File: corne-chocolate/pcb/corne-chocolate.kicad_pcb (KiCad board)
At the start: 2 copper layers, 133.8 x 91.4 mm, 98 parts, among them J1 MJ-4PP-9, J2 Conn_01x04, J3 LED, P1 i2c-pin, P2 i2c-pin, SW1 SW_PUSH, SW10 SW_PUSH, SW11 SW_PUSH, SW12 SW_PUSH, SW13 SW_PUSH, SW14 SW_PUSH, SW15 SW_PUSH, SW16 SW_PUSH, SW17 SW_PUSH, SW18 SW_PUSH, SW19 SW_PUSH, SW2 SW_PUSH, SW20 SW_PUSH, SW21 SW_PUSH, SW3 SW_PUSH, SW4 SW_PUSH, SW5 SW_PUSH, SW6 SW_PUSH, SW7 SW_PUSH, SW8 SW_PUSH, SW9 SW_PUSH, U1 ProMicro

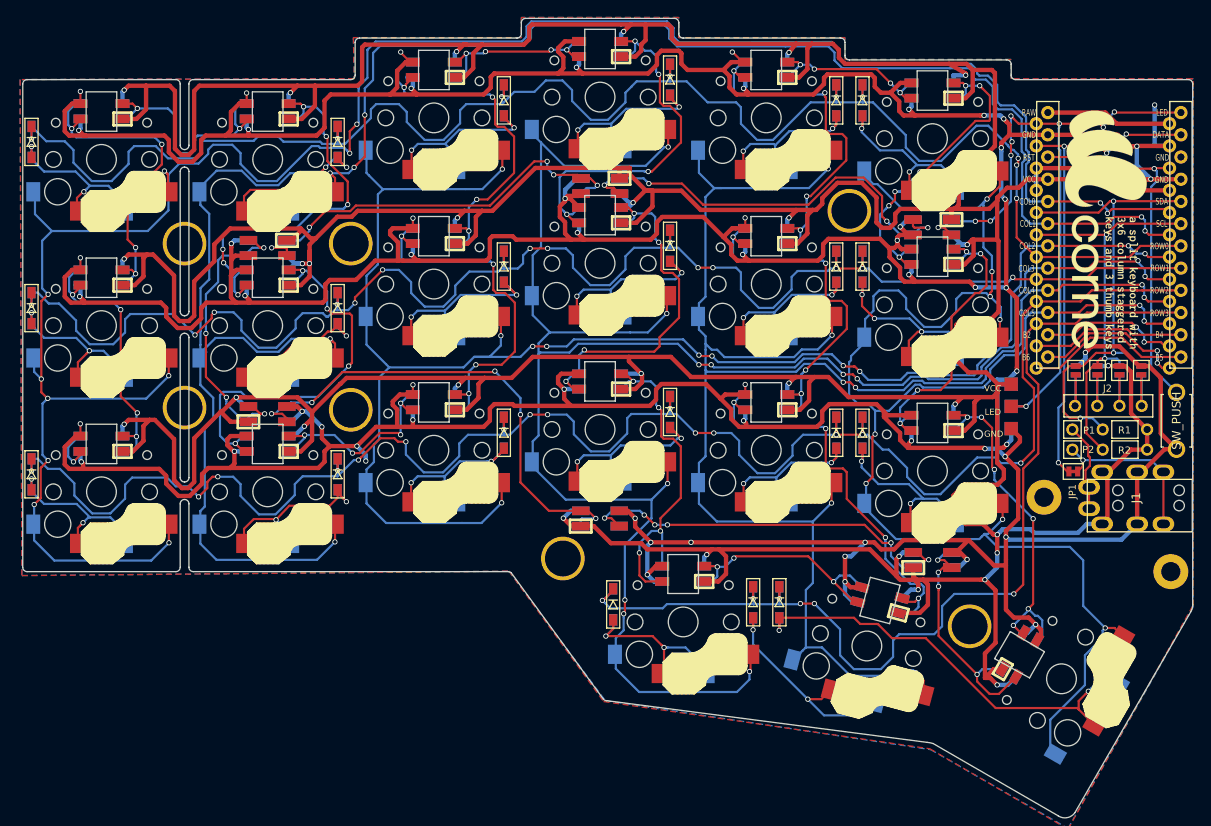
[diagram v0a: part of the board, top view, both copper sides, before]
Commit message: starts non-reversable pcbs routing
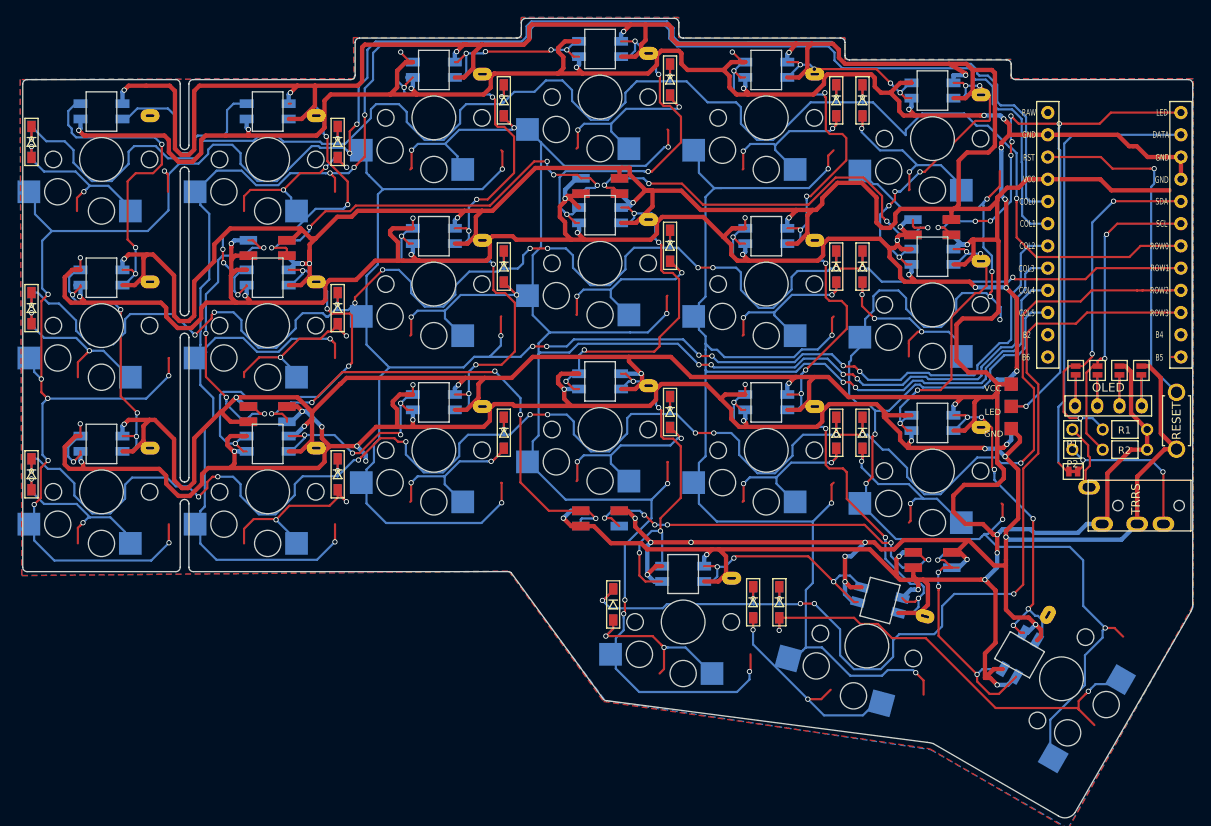
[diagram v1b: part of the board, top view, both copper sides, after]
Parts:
- removed ? (x9): , kbd:LEGO_HOLE
- removed G*** (x2): LOGO, kbd:corne
- removed JP6, JP7, JP8, JP9: , kbd:Jumper
- J1: footprint kbd:MJ-4PP-9 -> kbd:MJ-4PP-9_1side
- J2: footprint kbd:OLED -> kbd:OLED_1side
- J3: value LED -> Conn_01x03
- JP1: value (none) -> Device:Jumper
- JP2, JP3, JP4, JP5: value (none) -> Device:Jumper_NO_Small
- P1, P2: value i2c-pin -> Conn_01x01
- RSW1: footprint kbd:ResetSW -> kbd:ResetSW_1side
- SW1, SW10, SW11, SW12, SW13, SW14, SW15, SW16, SW17, SW18, SW19, SW2, SW20, SW3, SW4, SW5, SW6, SW7, SW8, SW9: footprint kbd:Choc_Hotswap -> kbd:ChocV1_V2_Hotswap
- SW21: footprint kbd:Choc_Hotswap_1.5u -> kbd:ChocV1_V2_Hotswap_1.5u
- U1: footprint kbd:ProMicro_v2 -> kbd:ProMicro_v2_1side
- turned SW1 to 0 degrees
- turned SW10 to 0 degrees
- turned SW11 to 0 degrees
- turned SW12 to 0 degrees
- turned SW13 to 0 degrees
- turned SW14 to 0 degrees
- turned SW15 to 0 degrees
- turned SW16 to 0 degrees
- turned SW17 to 0 degrees
- turned SW18 to 0 degrees
- turned SW19 to 0 degrees
- turned SW2 to 0 degrees
- turned SW20 to -15 degrees
- turned SW21 to 60 degrees
- turned SW3 to 0 degrees
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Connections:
- L13 pad 1: Net-(L13-Pad1) -> unconnected-(L13-DOUT-Pad1)
- U1 pad 11: Net-(U1-Pad11) -> unconnected-(U1-8/B4-Pad11)
- U1 pad 12: Net-(U1-Pad12) -> unconnected-(U1-9/B5-Pad12)
- U1 pad 13: Net-(U1-Pad13) -> unconnected-(U1-B6/10-Pad13)
- U1 pad 14: Net-(U1-Pad14) -> unconnected-(U1-B2/16-Pad14)
- U1 pad 24: Net-(U1-Pad24) -> unconnected-(U1-RAW-Pad24)
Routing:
- net (no net): track 0.00 -> 298.9 mm, vias 0 -> 35
- net GND: track 816.7 -> 759.8 mm, vias 59 -> 53
- net Net-(L14-DOUT): track 45.6 -> 0.00 mm, vias 4 -> 0
- net Net-(L2-DIN): track 46.2 -> 1.10 mm, vias 6 -> 0
- net Net-(L10-DOUT): track 42.9 -> 0.00 mm, vias 4 -> 0
- net Net-(L10-DIN): track 39.7 -> 0.00 mm, vias 4 -> 0
- net Net-(L16-DIN): track 39.3 -> 0.00 mm, vias 4 -> 0
- net Net-(L12-DOUT): track 37.0 -> 0.00 mm, vias 6 -> 0
- net Net-(L12-DIN): track 34.5 -> 0.00 mm, vias 4 -> 0
- net Net-(L5-DIN): track 19.8 -> 0.00 mm, vias 4 -> 0
- net Net-(U1-Pad12): track 18.9 -> 0.00 mm
- net col5: track 188.2 -> 170.3 mm, vias 10 -> 8
- net Net-(U1-Pad11): track 17.6 -> 0.00 mm
- net Net-(U1-Pad13): track 17.5 -> 0.00 mm, vias 2 -> 0
- net Net-(U1-Pad14): track 16.0 -> 0.00 mm, vias 2 -> 0
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
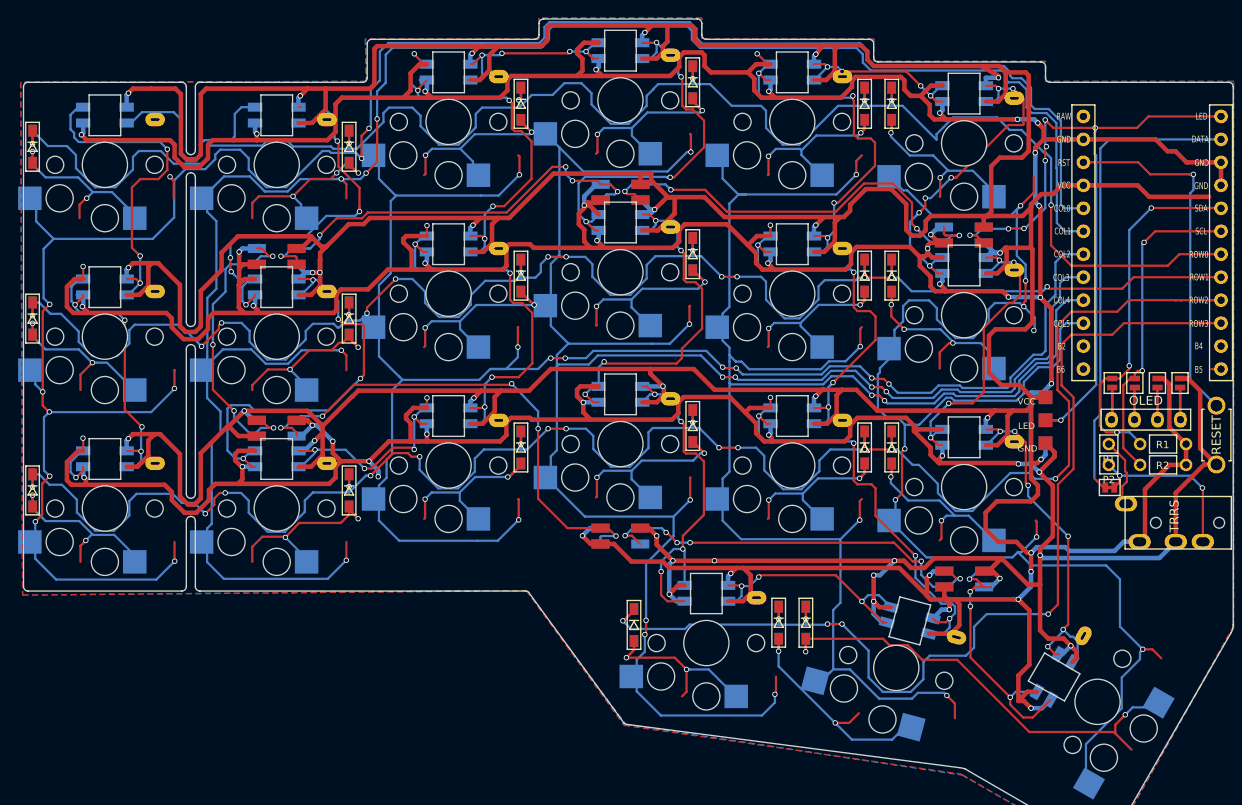
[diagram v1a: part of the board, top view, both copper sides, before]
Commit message: removes all reversible routing
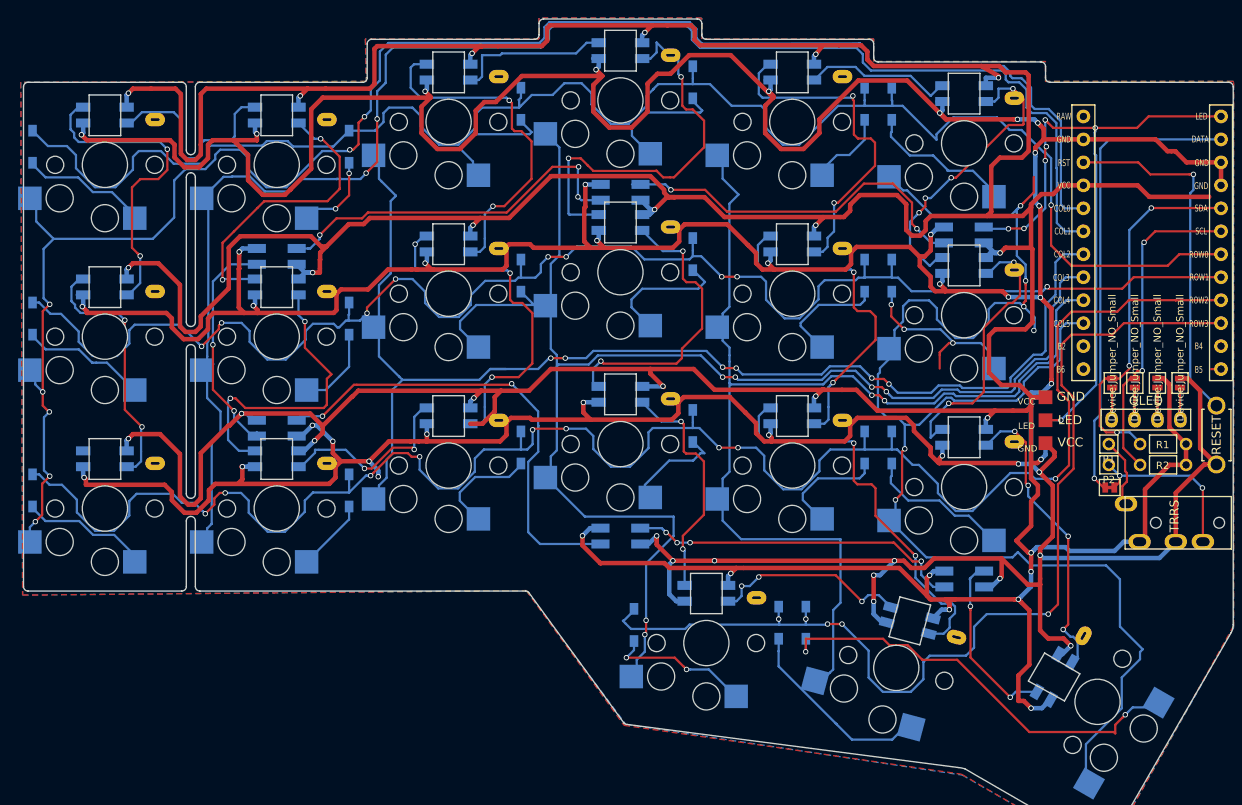
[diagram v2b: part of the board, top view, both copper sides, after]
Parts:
- J3: footprint kbd:StripLED_rev -> kbd:StripLED_1side
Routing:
- net (no net): track 298.9 -> 0.00 mm, vias 35 -> 0
- net VCC: track 777.0 -> 655.3 mm, vias 29 -> 28
- net GND: track 759.8 -> 691.4 mm, vias 53 -> 43
- net col3: track 209.1 -> 146.4 mm, vias 10 -> 6
- net col4: track 180.6 -> 122.5 mm, vias 6 -> 2
- net Net-(L10-DOUT): track 0.00 -> 44.4 mm, vias 0 -> 2
- net col2: track 178.9 -> 134.9 mm, vias 9 -> 6
- net col1: track 216.6 -> 172.8 mm, vias 5 -> 2
- net col0: track 239.8 -> 196.9 mm, vias 10 -> 7
- net Net-(L12-DOUT): track 0.00 -> 33.7 mm, vias 0 -> 4
- net Net-(L14-DOUT): track 0.00 -> 33.6 mm, vias 0 -> 2
- net Net-(L10-DIN): track 0.00 -> 32.2 mm, vias 0 -> 2
- net Net-(L2-DIN): track 1.10 -> 32.8 mm, vias 0 -> 2
- net Net-(L12-DIN): track 0.00 -> 30.9 mm, vias 0 -> 2
- net Net-(L16-DIN): track 0.00 -> 26.0 mm, vias 0 -> 2
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
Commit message: starts re-routing. switch to a 3x5 kbd
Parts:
- removed D1, D13, D7: D, kbd:D3_SMD
- removed L1, L13, L7: SK6812MINI, kbd:SK6812MINI_rev
- removed SW1, SW13, SW7: SW_PUSH, kbd:ChocV1_V2_Hotswap
- JP1: footprint kbd:JPC2 -> kbd:Jumper; moved to B.Cu
- moved JP1 1.16 mm to (180.0, 113.0)
- turned JP2 to 90 degrees
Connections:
- J1 pad B: Net-(P2-Pin_1) -> data
- JP1 pad 2: Net-(P2-Pin_1) -> data
- JP2 pad 1: GND -> Net-(J2-Pin_4)
- JP2 pad 2: Net-(J2-Pin_4) -> GND
- L2 pad 1: Net-(L1-DIN) -> unconnected-(L2-DOUT-Pad1)
- P2 pad 1: Net-(P2-Pin_1) -> data
- U1 pad 20: col0 -> unconnected-(U1-F4/A3-Pad20)
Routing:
- net VCC: track 655.3 -> 259.3 mm, vias 28 -> 2
- net GND: track 691.4 -> 340.3 mm, vias 43 -> 12
- net row2: track 199.8 -> 0.00 mm, vias 9 -> 0
- net col0: track 196.9 -> 0.00 mm, vias 7 -> 0
- net row3: track 114.4 -> 0.00 mm, vias 5 -> 0
- net col2: track 134.9 -> 39.0 mm, vias 6 -> 4
- net col5: track 163.2 -> 82.1 mm
- net col3: track 146.4 -> 68.4 mm
- net row1: track 172.3 -> 102.8 mm, vias 9 -> 0
- net row0: track 183.3 -> 115.1 mm, vias 1 -> 2
- net col4: track 122.5 -> 65.5 mm, vias 2 -> 6
- net Net-(L25-DOUT): track 52.9 -> 0.00 mm, vias 2 -> 0
- net Net-(D21-A): track 47.7 -> 0.00 mm, vias 2 -> 0
- net Net-(L10-DOUT): track 44.4 -> 0.00 mm, vias 2 -> 0
- net Net-(L17-DOUT): track 44.2 -> 0.00 mm, vias 2 -> 0
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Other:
- board size 133.8 x 91.4 mm -> 115.3 x 91.4 mm
- rule pad_to_mask_clearance: 0.2 -> 0.0508
- board text removed: "OLED"

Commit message: pcb with ohspark constraints
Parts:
- added G***: LOGO, kbd:corne-logo-horizontal, F.Cu at (106.7, 121.4)
- added H1: MountingHole, MountingHole:MountingHole_2.2mm_M2_ISO14580, F.Cu at (177.8, 115.8)
- added H2: MountingHole, MountingHole:MountingHole_2.2mm_M2_ISO14580, F.Cu at (192.3, 124.2)
- added H3: MountingHole, MountingHole:MountingHole_4.3mm_M4_ISO14580, F.Cu at (98.5, 86.8)
- added H4: MountingHole, MountingHole:MountingHole_4.3mm_M4_ISO14580, F.Cu at (155.5, 83.0)
- added H5: MountingHole, MountingHole:MountingHole_4.3mm_M4_ISO14580, F.Cu at (98.5, 105.8)
- added H6: MountingHole, MountingHole:MountingHole_4.3mm_M4_ISO14580, F.Cu at (122.8, 122.8)
- added H7: MountingHole, MountingHole:MountingHole_4.3mm_M4_ISO14580, F.Cu at (169.3, 130.5)
- L10, L11, L12, L14, L15, L16, L17, L18, L19, L2, L20, L21, L3, L4, L5, L6, L8, L9: footprint kbd:SK6812MINI_rev -> kbd:YS-SK6812MINI-E
- turned P1 to 90 degrees
- turned P2 to 180 degrees
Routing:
- net GND: track 340.3 -> 346.6 mm
- net VCC: track 259.3 -> 264.0 mm
- net col2: track 39.0 -> 40.5 mm
- net row1: track 102.8 -> 101.5 mm
- net col5: track 82.1 -> 83.0 mm
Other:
- board size 115.3 x 91.4 mm -> 116.2 x 91.4 mm
- board text added: "Corne Designed by foostan Remixed by ektocommers"
- board text removed: "Corne Chocolate v2.1 PCB designed by foostan"

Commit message: routing..
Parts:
- removed G***: LOGO, kbd:corne-logo-horizontal
- added kibuzzard-65BBD98A: G***, kibuzzard-65BBD98A, F.Cu at (106.3, 121.8)
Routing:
- net GND: track 346.6 -> 519.5 mm, vias 12 -> 15
- net VCC: track 264.0 -> 406.9 mm, vias 2 -> 7
- net col2: track 40.5 -> 152.6 mm, vias 4 -> 5
- net row2: track 0.00 -> 109.2 mm
- net row3: track 0.00 -> 90.6 mm
- net col3: track 68.2 -> 140.2 mm
- net col4: track 65.5 -> 114.4 mm, vias 6 -> 7
- net Net-(L22-DIN): track 0.50 -> 36.3 mm
- net Net-(L22-DOUT): track 0.00 -> 29.2 mm, vias 0 -> 2
- net Net-(L3-DOUT): track 0.00 -> 28.7 mm, vias 0 -> 2
- net col5: track 83.0 -> 111.2 mm, vias 6 -> 7
- net Net-(L11-DIN): track 0.00 -> 26.7 mm, vias 0 -> 2
- net Net-(L2-DIN): track 0.00 -> 25.8 mm, vias 0 -> 2
- net Net-(L14-DOUT): track 0.30 -> 24.2 mm, vias 0 -> 2
- net Net-(L10-DOUT): track 0.00 -> 23.7 mm, vias 0 -> 2
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
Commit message: more routing
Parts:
- JP1: moved to F.Cu
- turned JP1 to 180 degrees
- turned L25 to 0 degrees
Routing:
- net GND: track 519.5 -> 553.9 mm, vias 15 -> 16
- net data: track 55.6 -> 88.7 mm, vias 1 -> 0
- net Net-(L23-DIN): track 0.95 -> 33.4 mm
- net Net-(D10-A): track 0.00 -> 10.1 mm, vias 0 -> 2
- net VCC: track 406.9 -> 414.7 mm, vias 7 -> 6
- net reset: track 36.5 -> 39.7 mm
- net Net-(L22-DOUT): track 29.2 -> 31.9 mm
- net SDA: track 37.6 -> 38.8 mm
- net SCL: track 35.8 -> 37.0 mm

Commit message: all items connected
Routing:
- net VCC: track 414.7 -> 509.5 mm, vias 6 -> 12
- net GND: track 553.9 -> 646.8 mm, vias 16 -> 32
- net Net-(L25-DOUT): track 0.00 -> 52.6 mm, vias 0 -> 2
- net Net-(D21-A): track 0.00 -> 44.5 mm
- net Net-(L17-DOUT): track 0.00 -> 41.3 mm, vias 0 -> 2
- net Net-(L26-DOUT): track 0.00 -> 36.3 mm, vias 0 -> 2
- net Net-(L11-DOUT): track 0.00 -> 29.9 mm, vias 0 -> 2
- net Net-(L18-DIN): track 0.00 -> 29.3 mm, vias 0 -> 2
- net Net-(L12-DOUT): track 0.00 -> 29.2 mm, vias 0 -> 2
- net Net-(L15-DIN): track 0.00 -> 29.0 mm, vias 0 -> 2
- net Net-(L10-DIN): track 0.00 -> 25.3 mm, vias 0 -> 2
- net Net-(L16-DIN): track 0.00 -> 23.3 mm, vias 0 -> 2
- net Net-(D20-A): track 0.00 -> 21.7 mm
- net Net-(L12-DIN): track 0.00 -> 21.4 mm, vias 0 -> 2
- net Net-(L21-DIN): track 0.00 -> 21.3 mm, vias 0 -> 2
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
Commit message: more routing
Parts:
- moved L26 0.76 mm to (127.6, 118.7)
- turned L21 to 60 degrees
- turned L27 to 0 degrees
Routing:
- net Net-(D21-A): track 44.5 -> 57.8 mm
- net GND: track 646.8 -> 639.5 mm, vias 32 -> 42
- net Net-(L26-DOUT): track 36.3 -> 39.9 mm, vias 2 -> 0
- net LED: track 63.6 -> 66.7 mm, vias 1 -> 3
- net Net-(L12-DOUT): track 29.2 -> 26.4 mm
- net Net-(L3-DOUT): track 28.7 -> 31.2 mm
- net VCC: track 509.5 -> 511.7 mm, vias 12 -> 23
- net Net-(L18-DIN): track 29.3 -> 31.3 mm
- net row3: track 91.4 -> 92.7 mm, vias 0 -> 2
- net col4: track 114.2 -> 115.5 mm
- net Net-(D9-A): track 8.07 -> 9.22 mm
- net Net-(L25-DOUT): track 52.6 -> 53.6 mm, vias 2 -> 0
- net Net-(L23-DIN): track 39.2 -> 40.1 mm
- net Net-(L21-DIN): track 21.3 -> 20.4 mm
- net Net-(D20-A): track 21.7 -> 22.5 mm
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- added copper zone on F.Cu, net LED
- added copper zone on B.Cu, net Net-(D18-A)
- added copper zone on B.Cu, net Net-(L12-DIN)
- added copper zone on B.Cu, net Net-(L14-DOUT)
- added copper zone on B.Cu, net VCC
- added copper zone on F.Cu, net VCC
- added copper zone on F.Cu, net col4
- added copper zone on B.Cu, net row2
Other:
- board text added: "Designed by foostan Remixed by ektocommers"
- board text removed: "Corne Designed by foostan Remixed by ektocommers"
